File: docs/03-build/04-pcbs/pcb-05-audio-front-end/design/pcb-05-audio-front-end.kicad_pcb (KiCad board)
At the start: 2 copper layers, 30 x 38 mm, 0 parts

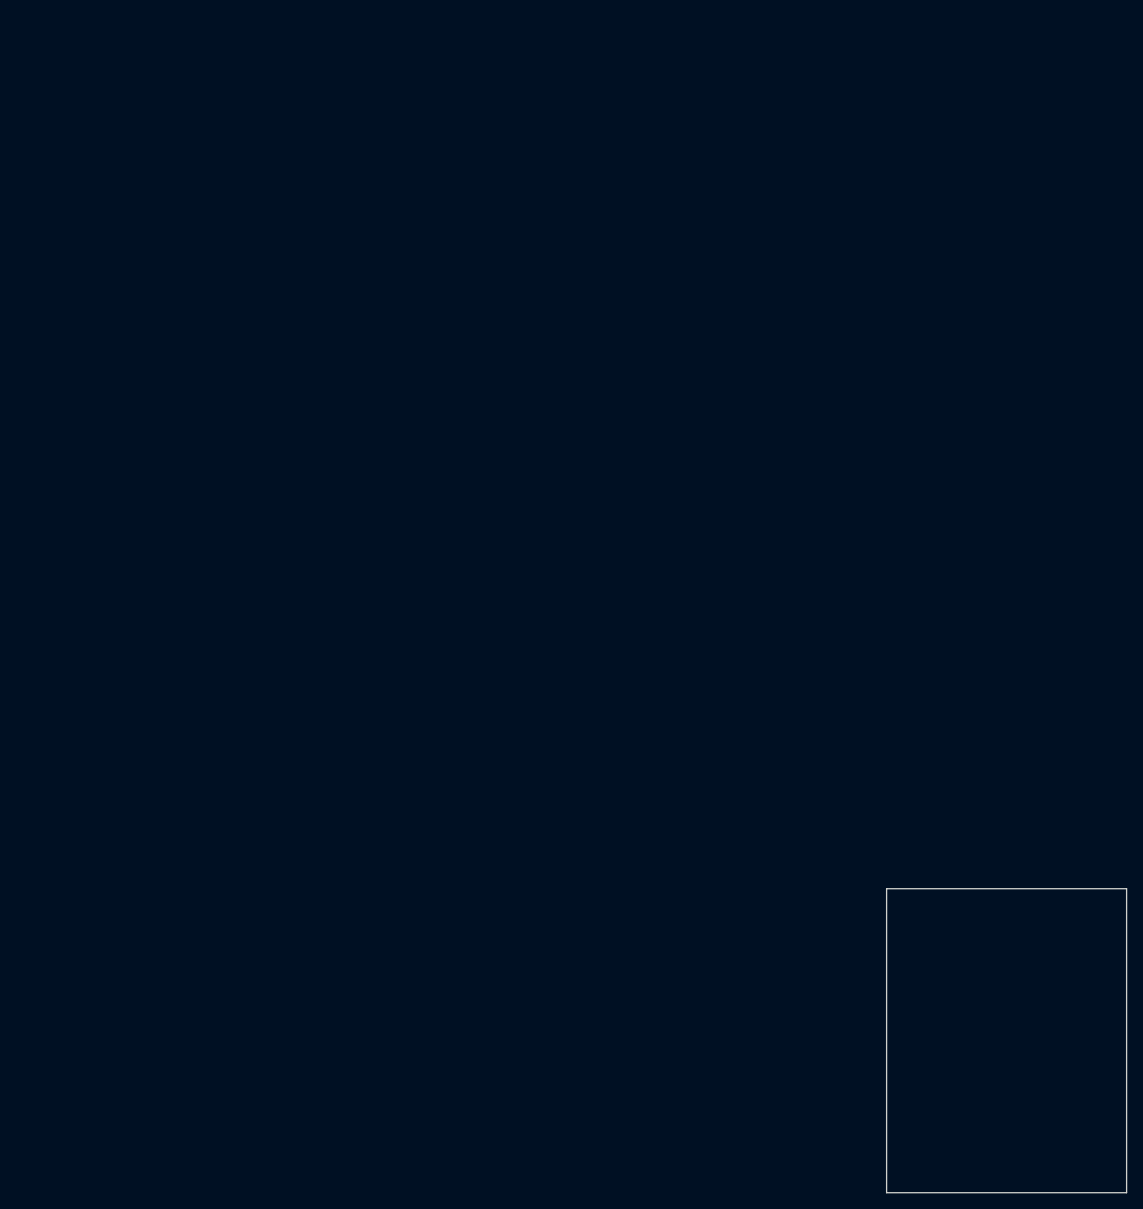
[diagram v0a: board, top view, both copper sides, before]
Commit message: build(pcbs): PCB-05 placed and routed on 4 layers, DRC clean (D-067 amended, lesson 4)
Placement found the lesson-1 fixing on the GH pads (J1: one rear, two front
spacers; J5-1 2 mm toward -Y; J5-7 at its real 9.65 mm width; mount check 7/7).
Routing the left half needed 4 layers (L2: In1 solid GND, In2 GND + slow rows,
B.Cu clock bus) and a J5-1 reorder (LRCLK above BCLK; SDI1 above SDI0).
DRC 0 errors, 0 unconnected, parity clean; 30 cosmetic lib_footprint_mismatch.
kp.py: library_models() reads one-line (model ...) entries (U1/U2 had lost
their models); remove_in() helper. Playbook: four more PCB-05 traps.

Co-Authored-By: Claude Opus 5.5 <noreply@anthropic.com>
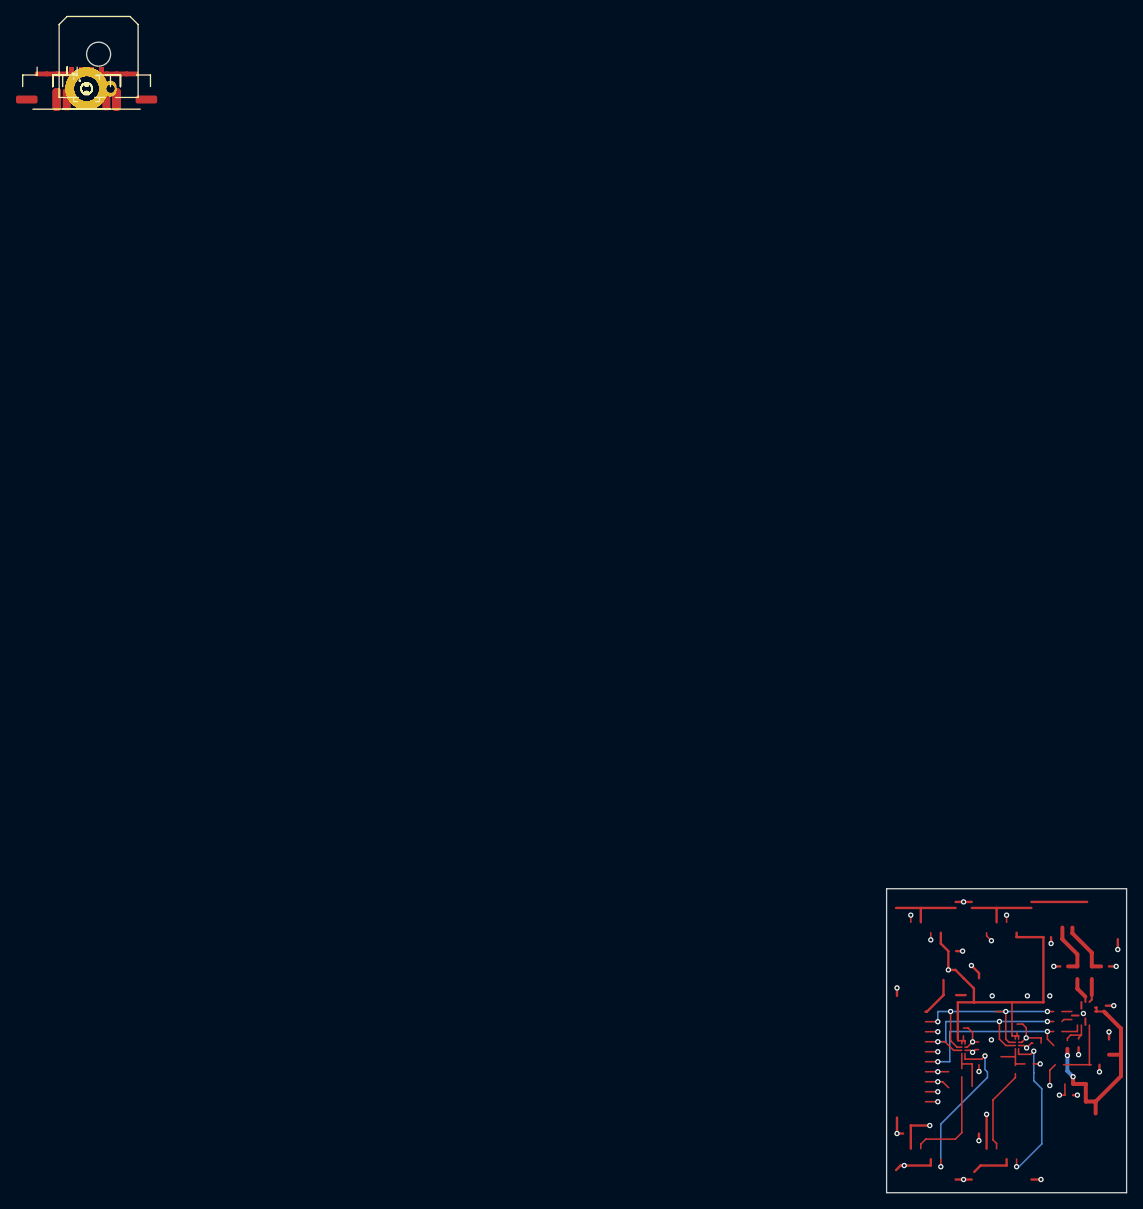
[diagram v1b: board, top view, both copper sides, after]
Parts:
- added C1: 10u X5R 10V, Capacitor_SMD:C_0805_2012Metric, F.Cu at (0.00, 0.00)
- added C10, C11: DNP 1n, Capacitor_SMD:C_0402_1005Metric, F.Cu at (0.00, 0.00)
- added C2, C3, C4, C5, C6, C7: 100n X7R 10V, Capacitor_SMD:C_0402_1005Metric, F.Cu at (0.00, 0.00)
- added C8: 10u X5R 16V, Capacitor_SMD:C_0805_2012Metric, F.Cu at (0.00, 0.00)
- added C9: 100n X7R 16V, Capacitor_SMD:C_0402_1005Metric, F.Cu at (0.00, 0.00)
- added FB1: 600R@100MHz, Inductor_SMD:L_0603_1608Metric, F.Cu at (0.00, 0.00)
- added FB2, FB3: 0R (or ferrite), Inductor_SMD:L_0603_1608Metric, F.Cu at (0.00, 0.00)
- added H1, H2, H3: 9774080243R, pcb05:Wurth_WA-SMSI-M2_H8mm_9774080243_PTH, F.Cu at (0.00, 0.00)
- added J1: J5-1 host (W26), Connector_JST:JST_GH_SM10B-GHS-TB_1x10-1MP_P1.25mm_Horizontal, F.Cu at (0.00, 0.00)
- added J2: J5-2 REAR_L, Connector_JST:JST_GH_SM04B-GHS-TB_1x04-1MP_P1.25mm_Horizontal, F.Cu at (0.00, 0.00)
- added J3: J5-3 FRONT_L, Connector_JST:JST_GH_SM04B-GHS-TB_1x04-1MP_P1.25mm_Horizontal, F.Cu at (0.00, 0.00)
- added J4: J5-4 REAR_R, Connector_JST:JST_GH_SM04B-GHS-TB_1x04-1MP_P1.25mm_Horizontal, F.Cu at (0.00, 0.00)
- added J5: J5-5 FRONT_R, Connector_JST:JST_GH_SM04B-GHS-TB_1x04-1MP_P1.25mm_Horizontal, F.Cu at (0.00, 0.00)
- added J6: J5-6 speaker (W28), Connector_JST:JST_GH_SM02B-GHS-TB_1x02-1MP_P1.25mm_Horizontal, F.Cu at (0.00, 0.00)
- added J7: J5-7 +5 V (W12), Connector_Molex:Molex_Micro-Fit_3.0_43650-0200_1x02_P3.00mm_Horizontal, F.Cu at (0.00, 0.00)
- added R1: 2.2, Resistor_SMD:R_0402_1005Metric, F.Cu at (0.00, 0.00)
- added R10, R2, R3, R4, R5, R8, R9: 100, Resistor_SMD:R_0402_1005Metric, F.Cu at (0.00, 0.00)
- added R11: 2.2k, Resistor_SMD:R_0402_1005Metric, F.Cu at (0.00, 0.00)
- added R12, R6, R7: 100k, Resistor_SMD:R_0402_1005Metric, F.Cu at (0.00, 0.00)
- added R13, R14: DNP, Resistor_SMD:R_0402_1005Metric, F.Cu at (0.00, 0.00)
- added R15: DNP 10k, Resistor_SMD:R_0402_1005Metric, F.Cu at (0.00, 0.00)
- added R16: DNP 15k, Resistor_SMD:R_0402_1005Metric, F.Cu at (0.00, 0.00)
- added TP1: BCLK, TestPoint:TestPoint_Pad_D1.0mm, F.Cu at (0.00, 0.00)
- added TP10: +3V3_MIC, TestPoint:TestPoint_Pad_D1.0mm, F.Cu at (0.00, 0.00)
- added TP11: +5V_AMP, TestPoint:TestPoint_Pad_D1.0mm, F.Cu at (0.00, 0.00)
- added TP12: GND, TestPoint:TestPoint_Pad_D1.0mm, F.Cu at (0.00, 0.00)
- added TP2: LRCLK, TestPoint:TestPoint_Pad_D1.0mm, F.Cu at (0.00, 0.00)
- added TP3: SDI0, TestPoint:TestPoint_Pad_D1.0mm, F.Cu at (0.00, 0.00)
- added TP4: SDI1, TestPoint:TestPoint_Pad_D1.0mm, F.Cu at (0.00, 0.00)
- added TP5: SDO0, TestPoint:TestPoint_Pad_D1.0mm, F.Cu at (0.00, 0.00)
- added TP6: AMP_SD, TestPoint:TestPoint_Pad_D1.0mm, F.Cu at (0.00, 0.00)
- added TP7: PDM_CLK1, TestPoint:TestPoint_Pad_D1.0mm, F.Cu at (0.00, 0.00)
- added TP8: PDM_CLK2, TestPoint:TestPoint_Pad_D1.0mm, F.Cu at (0.00, 0.00)
- added TP9: +3V3, TestPoint:TestPoint_Pad_D1.0mm, F.Cu at (0.00, 0.00)
- added U1, U2: ADAU7002ACBZ-R7, pcb05:ADAU7002_WLCSP-8_0.76x1.56mm_P0.4mm, F.Cu at (0.00, 0.00)
- added U3: MAX98357AETE+T, Package_DFN_QFN:TQFN-16-1EP_3x3mm_P0.5mm_EP1.23x1.23mm, F.Cu at (0.00, 0.00)
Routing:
- net /+3V3_MIC: track 0.00 -> 84.6 mm, vias 0 -> 3
- net /GND: track 0.00 -> 73.4 mm, vias 0 -> 27
- net /PDM_DAT2: track 0.00 -> 48.5 mm, vias 0 -> 3
- net /PDM_DAT1: track 0.00 -> 40.4 mm, vias 0 -> 3
- net /LRCLK: track 0.00 -> 28.8 mm, vias 0 -> 4
- net /+5V_AMP: track 0.00 -> 28.0 mm, vias 0 -> 2
- net /BCLK: track 0.00 -> 26.5 mm, vias 0 -> 3
- net /CLK_FL: track 0.00 -> 24.7 mm, vias 0 -> 2
- net /CLK_RL: track 0.00 -> 24.2 mm, vias 0 -> 2
- net /SDO0: track 0.00 -> 21.9 mm, vias 0 -> 2
- net /SDI0: track 0.00 -> 20.7 mm, vias 0 -> 2
- net /5V_SENSE: track 0.00 -> 19.2 mm, vias 0 -> 2
- net /AMP_SD: track 0.00 -> 18.8 mm, vias 0 -> 2
- net /CLK_RR: track 0.00 -> 13.3 mm
- net /SDI1: track 0.00 -> 11.6 mm, vias 0 -> 2
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- added copper zone on In1.Cu, net /GND
- added copper zone on In2.Cu, net /GND
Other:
- copper layers 2 -> 4
- board text added: "H2 plated"
- board text added: "H3 plated"
- board text removed: "H3 plated hole (I1)"

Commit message: build(pcbs): PCB-05 audio front end rev A; fit check passes (lesson 5)
Board STEP with every part: U3's TQFN and J7's Micro-Fit named models KiCad
doesn't ship, so both use project footprint copies (J7's model from Molex's
dimensions, tails clipped per D-067 H1). Fab outputs in fab/revA: 4-layer
Gerbers, drill, BOM, placement and JLCPCB CPL from the board-local origin, zip
and order parameters. check_pcb05_fit.py places the STEP in the droid: 8/8
(J7 housing 0.98 under the front boss, clipped tails 1.63 above the Pi's USB
jack, install slide 0.46). kp.audit() now checks model files exist.

Co-Authored-By: Claude Opus 5.5 <noreply@anthropic.com>
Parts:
- J7: footprint Connector_Molex:Molex_Micro-Fit_3.0_43650-0200_1x02_P3.00mm_Horizontal -> pcb05:Molex_Micro-Fit_3.0_43650-0200_1x02_P3.00mm_Horizontal
- U3: footprint Package_DFN_QFN:TQFN-16-1EP_3x3mm_P0.5mm_EP1.23x1.23mm -> pcb05:TQFN-16-1EP_3x3mm_P0.5mm_EP1.23x1.23mm
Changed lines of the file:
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@@
 		)
 	)
-	(footprint "Package_DFN_QFN:TQFN-16-1EP_3x3mm_P0.5mm_EP1.23x1.23mm"
+	(footprint "pcb05:TQFN-16-1EP_3x3mm_P0.5mm_EP1.23x1.23mm"
 		(layer "F.Cu")
 		(transform
@@
 		)
 		(embedded_fonts no)
-		(model "${KICAD10_3DMODEL_DIR}/Package_DFN_QFN.3dshapes/TQFN-16-1EP_3x3mm_P0.5mm_EP1.23x1.23mm.step"
+		(model "${KICAD10_3DMODEL_DIR}/Package_DFN_QFN.3dshapes/TQFN-16-1EP_3x3mm_P0.5mm_EP1.6x1.6mm.step"
 			(offset
 				(xyz 0 0 0)
@@
 		(embedded_fonts no)
 	)
-	(footprint "Connector_Molex:Molex_Micro-Fit_3.0_43650-0200_1x02_P3.00mm_Horizontal"
+	(footprint "pcb05:Molex_Micro-Fit_3.0_43650-0200_1x02_P3.00mm_Horizontal"
 		(layer "F.Cu")
 		(transform
@@
 		)
 		(embedded_fonts no)
-		(model "${KICAD10_3DMODEL_DIR}/Connector_Molex.3dshapes/Molex_Micro-Fit_3.0_43650-0200_1x02_P3.00mm_Horizontal.step"
+		(model "${KIPRJMOD}/pcb05.3dshapes/Molex_Micro-Fit_3.0_43650-0200_clipped.step"
 			(offset
 				(xyz 0 0 0)
